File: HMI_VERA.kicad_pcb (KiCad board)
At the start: 2 copper layers, 100 x 60 mm, 34 parts, among them J1 Conn_01x03, J2 Conn_01x03, J3 Conn_01x03, J4 Conn_01x03, J8 Conn_01x03, J9 DB9_Female, U1 THD10-1211N, U2 LM1117-3.3, U3 MAX3232, U4 RPI_3B+_Pinout_With_RUN

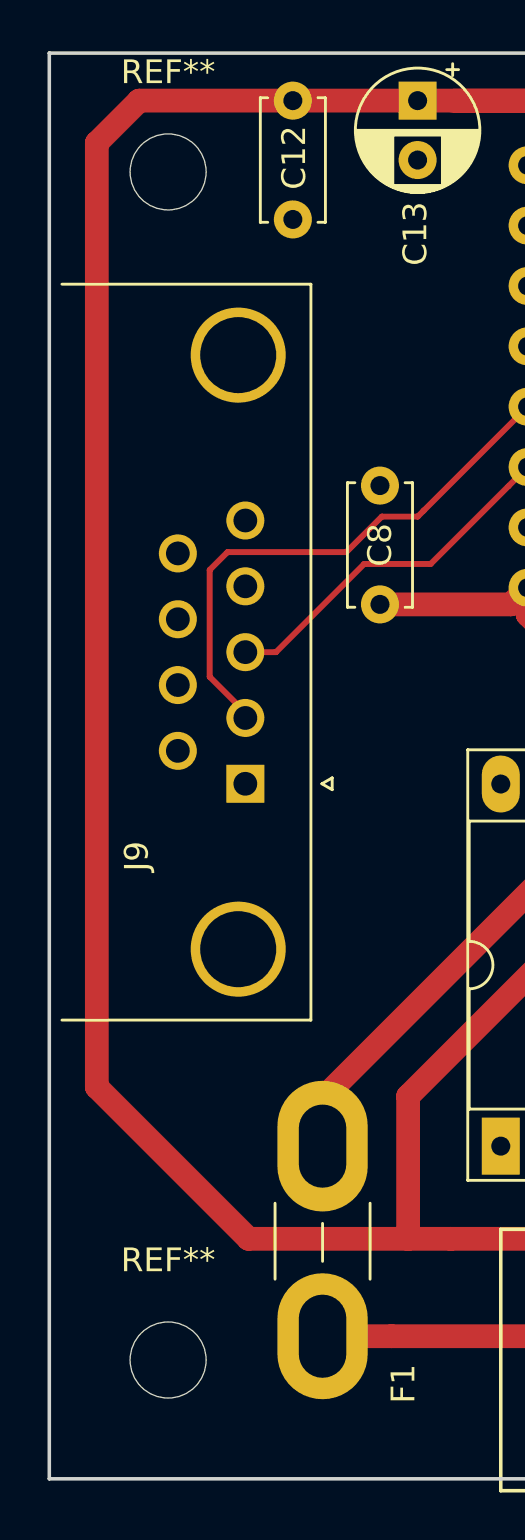
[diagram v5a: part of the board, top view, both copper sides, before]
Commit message: Add BOM and assign component product codes.
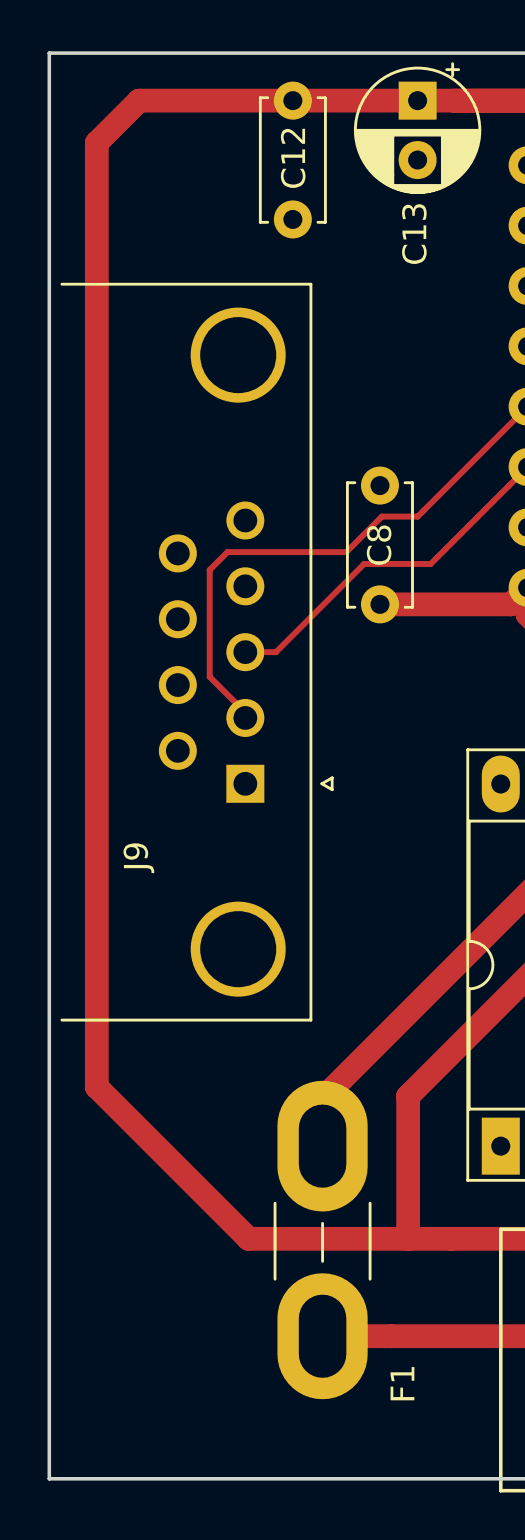
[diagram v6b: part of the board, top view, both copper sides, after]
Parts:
- removed REF** (x2): MountingHole_3.2mm_M3, Mounting_Holes:MountingHole_3.2mm_M3
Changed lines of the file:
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@@
     (tracks 195)
     (zones 0)
-    (modules 34)
+    (modules 32)
     (nets 65)
   )
@@
     (add_net "Net-(J8-Pad2)")
   )
-  (module Mounting_Holes:MountingHole_3.2mm_M3 (layer F.Cu)
-    (at 82 113)
-    (descr "Mounting Hole 3.2mm, no annular, M3")
-    (tags "mounting hole 3.2mm no annular m3")
-    (attr virtual)
-    (fp_text reference REF** (at 0 -4.2) (layer F.SilkS)
-      (effects (font (size 1 1) (thickness 0.15)))
-    )
-    (fp_text value MountingHole_3.2mm_M3 (at 0 4.2) (layer F.Fab)
-      (effects (font (size 1 1) (thickness 0.15)))
-    )
-    (fp_text user %R (at 0.3 0) (layer F.Fab)
-      (effects (font (size 1 1) (thickness 0.15)))
-    )
-    (fp_circle (center 0 0) (end 3.2 0) (layer Cmts.User) (width 0.15))
-    (fp_circle (center 0 0) (end 3.45 0) (layer F.CrtYd) (width 0.05))
-    (pad 1 np_thru_hole circle (at 0 0) (size 3.2 3.2) (drill 3.2) (layers *.Cu *.Mask))
-  )
-  (module Mounting_Holes:MountingHole_3.2mm_M3 (layer F.Cu)
-    (at 82 63)
-    (descr "Mounting Hole 3.2mm, no annular, M3")
-    (tags "mounting hole 3.2mm no annular m3")
-    (attr virtual)
-    (fp_text reference REF** (at 0 -4.2) (layer F.SilkS)
-      (effects (font (size 1 1) (thickness 0.15)))
-    )
-    (fp_text value MountingHole_3.2mm_M3 (at 0 4.2) (layer F.Fab)
-      (effects (font (size 1 1) (thickness 0.15)))
-    )
-    (fp_text user %R (at 0.3 0) (layer F.Fab)
-      (effects (font (size 1 1) (thickness 0.15)))
-    )
-    (fp_circle (center 0 0) (end 3.2 0) (layer Cmts.User) (width 0.15))
-    (fp_circle (center 0 0) (end 3.45 0) (layer F.CrtYd) (width 0.05))
-    (pad 1 np_thru_hole circle (at 0 0) (size 3.2 3.2) (drill 3.2) (layers *.Cu *.Mask))
-  )
   (module Resistors_THT:R_Axial_DIN0207_L6.3mm_D2.5mm_P10.16mm_Horizontal (layer F.Cu)
     (at 165.75 94.15 270)
@@
   (segment (start 147.5 105.75) (end 149 104.25) (width 0.25) (layer F.Cu) (net 14) (status 20))
   (segment (start 147.5 109) (end 147.5 105.75) (width 0.25) (layer F.Cu) (net 14) (status 10))
-  (segment (start 175.28 79.58) (end 175.28 77.43) (width 0.25) (layer F.Cu) (net 15))
+  (segment (start 175.28 79.58) (end 175.28 77.43) (width 0.25) (layer F.Cu) (net 15) (status 20))
   (segment (start 169.475 105.225) (end 169.475 85.385) (width 0.25) (layer F.Cu) (net 15))
   (segment (start 169.475 85.385) (end 175.28 79.58) (width 0.25) (layer F.Cu) (net 15))
-  (segment (start 163.5 109) (end 165.7 109) (width 0.25) (layer F.Cu) (net 15))
+  (segment (start 163.5 109) (end 165.7 109) (width 0.25) (layer F.Cu) (net 15) (status 10))
   (segment (start 165.7 109) (end 169.475 105.225) (width 0.25) (layer F.Cu) (net 15))
-  (segment (start 161.31 85.19) (end 161.31 66) (width 0.25) (layer F.Cu) (net 16))
-  (segment (start 161 109) (end 161 107.444366) (width 0.25) (layer F.Cu) (net 16))
+  (segment (start 161.31 85.19) (end 161.31 66) (width 0.25) (layer F.Cu) (net 16) (status 20))
+  (segment (start 161 109) (end 161 107.444366) (width 0.25) (layer F.Cu) (net 16) (status 10))
   (segment (start 166.5 106.75) (end 168.275 104.975) (width 0.25) (layer F.Cu) (net 16))
   (segment (start 161 107.444366) (end 161.694366 106.75) (width 0.25) (layer F.Cu) (net 16))
@@
   (segment (start 138.45 67.95) (end 145.35 74.85) (width 0.25) (layer F.Cu) (net 28))
   (segment (start 157 68.75) (end 156.23 67.98) (width 0.25) (layer F.Cu) (net 29))
-  (segment (start 158.754 94.148) (end 157 92.394) (width 0.25) (layer F.Cu) (net 29))
-  (segment (start 156.23 67.98) (end 156.23 66) (width 0.25) (layer F.Cu) (net 29))
+  (segment (start 158.754 94.148) (end 157 92.394) (width 0.25) (layer F.Cu) (net 29) (status 10))
+  (segment (start 156.23 67.98) (end 156.23 66) (width 0.25) (layer F.Cu) (net 29) (status 20))
   (segment (start 157 92.394) (end 157 68.75) (width 0.25) (layer F.Cu) (net 29))
   (segment (start 152.09 94.09) (end 152.1 94.1) (width 0.25) (layer F.Cu) (net 30) (status 30))
   (segment (start 149 94.09) (end 152.09 94.09) (width 0.25) (layer F.Cu) (net 30) (status 30))
-  (segment (start 152.1 90.15) (end 152.1 94.1) (width 0.25) (layer F.Cu) (net 30))
+  (segment (start 152.1 90.15) (end 152.1 94.1) (width 0.25) (layer F.Cu) (net 30) (status 20))
   (segment (start 156 86.25) (end 152.1 90.15) (width 0.25) (layer F.Cu) (net 30))
   (segment (start 156 70.5) (end 156 86.25) (width 0.25) (layer F.Cu) (net 30))
-  (segment (start 153.69 66) (end 153.69 68.19) (width 0.25) (layer F.Cu) (net 30))
+  (segment (start 153.69 66) (end 153.69 68.19) (width 0.25) (layer F.Cu) (net 30) (status 10))
   (segment (start 153.69 68.19) (end 156 70.5) (width 0.25) (layer F.Cu) (net 30))
   (segment (start 127.440001 64.309999) (end 128.29 63.46) (width 0.25) (layer F.Cu) (net 34) (status 30))
@@
   (segment (start 102.055634 112) (end 91.4 112) (width 1) (layer F.Cu) (net 59))
   (segment (start 103.5 109) (end 103.5 110.555634) (width 1) (layer F.Cu) (net 59) (status 10))
-  (segment (start 162.25 104.55) (end 162.25 104.31) (width 0.25) (layer F.Cu) (net 62))
-  (segment (start 158.5 109) (end 158.5 108.3) (width 0.25) (layer F.Cu) (net 62))
-  (segment (start 158.5 108.3) (end 162.25 104.55) (width 0.25) (layer F.Cu) (net 62))
-  (segment (start 162.25 91.35) (end 162.25 94.15) (width 0.25) (layer F.Cu) (net 63))
-  (segment (start 158.77 66) (end 158.77 87.87) (width 0.25) (layer F.Cu) (net 63))
+  (segment (start 162.25 104.55) (end 162.25 104.31) (width 0.25) (layer F.Cu) (net 62) (status 30))
+  (segment (start 158.5 109) (end 158.5 108.3) (width 0.25) (layer F.Cu) (net 62) (status 30))
+  (segment (start 158.5 108.3) (end 162.25 104.55) (width 0.25) (layer F.Cu) (net 62) (status 30))
+  (segment (start 162.25 91.35) (end 162.25 94.15) (width 0.25) (layer F.Cu) (net 63) (status 20))
+  (segment (start 158.77 66) (end 158.77 87.87) (width 0.25) (layer F.Cu) (net 63) (status 10))
   (segment (start 158.77 87.87) (end 162.25 91.35) (width 0.25) (layer F.Cu) (net 63))
-  (segment (start 165.75 94.15) (end 162.25 94.15) (width 0.25) (layer F.Cu) (net 63))
+  (segment (start 165.75 94.15) (end 162.25 94.15) (width 0.25) (layer F.Cu) (net 63) (status 30))
   (zone (net 2) (net_name GND) (layer B.Cu) (hatch edge 0.508)
     (connect_pads (clearance 0.508))
